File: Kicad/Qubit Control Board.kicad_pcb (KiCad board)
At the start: 6 copper layers, 144 x 81.5 mm, 149 parts, among them J1 USB_C_Receptacle_PowerOnly_6P, J2 CLK_Pins, J3 Idata, J4 Qdata, J5 SPIdata, J6 SMA, U1 LT3045xMSE, U2 TRF372017IRGZR, U3 LT3045xMSE, U4 LT3045xMSE, U5 SN65LVDS1DBV, U6 AD9743BCPZ, Y1 SiT8008xx-3x-xxN, Y2 CVHD-950-100.000

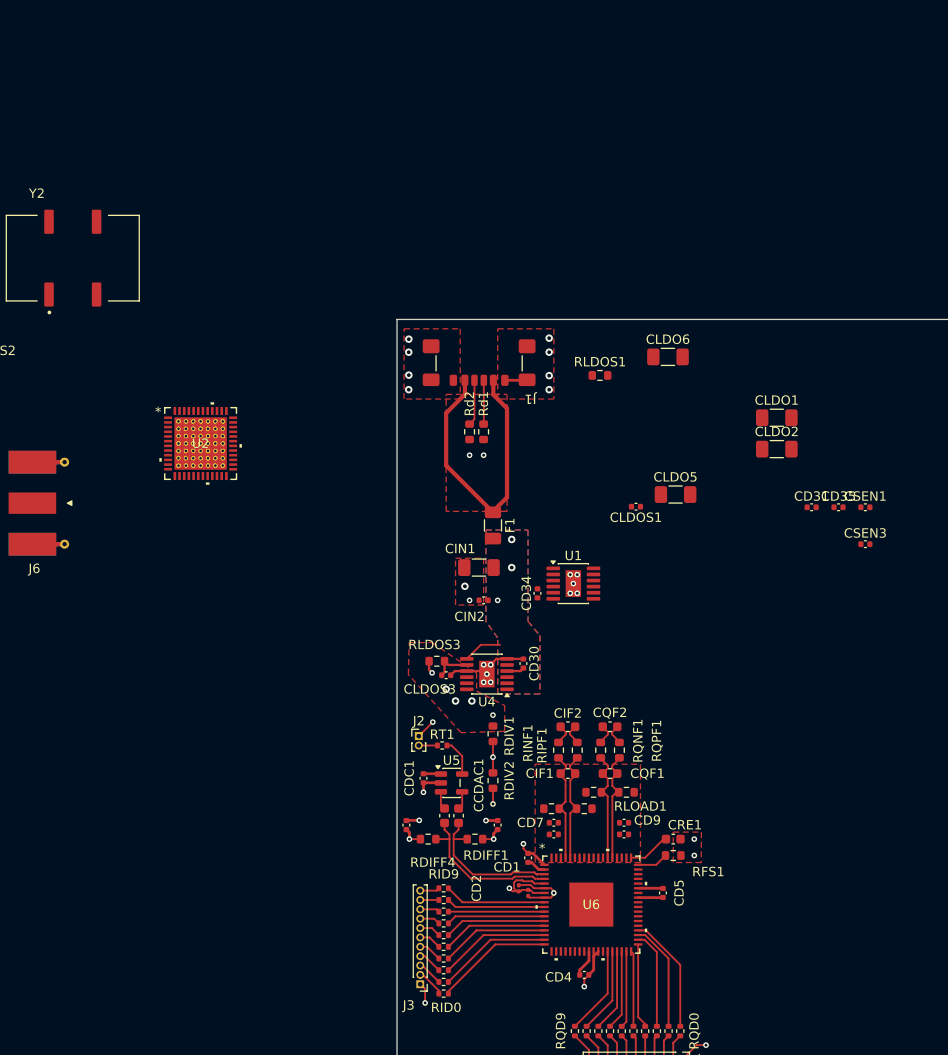
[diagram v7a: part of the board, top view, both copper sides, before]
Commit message: 3.3V-A LDO
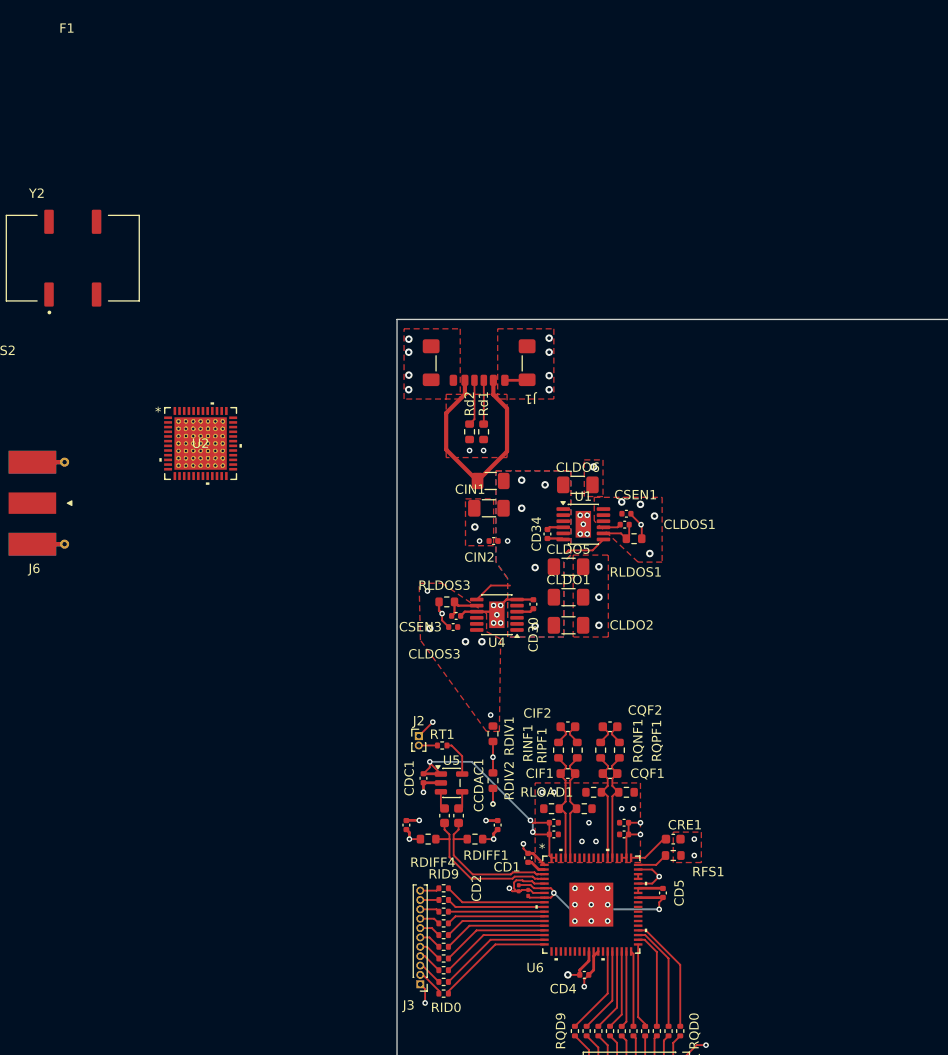
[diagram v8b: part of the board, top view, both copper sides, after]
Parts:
- removed CD31, CD35: 100n, Capacitor_SMD:C_0402_1005Metric
- CD29: value 1n -> 100n
- moved CSEN3 44.9 mm to (112.5, 68.8)
- moved CLDO1 29.4 mm to (124.8, 65.7)
- moved CLDO2 29.1 mm to (124.8, 68.7)
- moved CSEN1 25.5 mm to (131.0, 56.8), turned to 180 degrees
- moved RLDOS1 17.8 mm to (131.8, 59.4), turned to 180 degrees
- moved CLDO6 16.7 mm to (125.8, 53.7)
- moved CLDO5 13.8 mm to (124.8, 62.4)
- moved CD34 6.42 mm to (122.6, 58.9)
- moved CIN1 6.42 mm to (116.3, 56.2)
- moved CIN2 6.42 mm to (116.8, 59.7)
- moved U1 6.42 mm to (126.4, 57.9)
- moved U4 6.42 mm to (117.2, 67.5)
- moved CD30 6.42 mm to (121.1, 66.4)
- moved CLDOS3 6.42 mm to (112.8, 67.7)
- moved RLDOS3 6.42 mm to (111.8, 66.2)
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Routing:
- net +3.3V-A: track 4.78 -> 44.4 mm, vias 0 -> 11
- net +1.8V: track 13.5 -> 27.1 mm, vias 6 -> 8
- net GND: track 46.5 -> 56.0 mm, vias 34 -> 55
- net Net-(CD28-Pad2): track 10.4 -> 19.1 mm
- net Net-(F1-Pad1): track 32.4 -> 25.6 mm
- net +5V: track 6.05 -> 12.4 mm, vias 3 -> 6
- net Net-(U1-SET): track 0.00 -> 4.30 mm
- added copper zone on F.Cu, net +3.3V-A
- added copper zone on In4.Cu, net +3.3V-A
